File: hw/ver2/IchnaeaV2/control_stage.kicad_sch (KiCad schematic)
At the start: 119 parts, among them J5 FanConnector, J6 BMS_Serial, P1 USB_C_Plug_USB2.0, Q26 BSS138, Q27 BSS84, Q28 BSS138, Q29 BSS138, Q30 BSS138, SW1 Boot, SW2 Reset, U10 W25Q32JVZP, U11 RP2040, U12 LM1117MP-5.0, U13 LM1117MP-3.3, U14 W25Q32JVZP, U9 74HC4051PW, Y1 12MHz

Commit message: Partial pin mapping. ESD protection on signals that exit the board.
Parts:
- removed R85: 1k, Resistor_SMD:R_0603_1608Metric, symbol Device:R_US
- added C111: 100nF, Capacitor_SMD:C_0603_1608Metric, symbol Device:C
- added D11, D12, D13, D14, D15, D16, D17, D18, D9: ESD9B3.3ST5G, Diode_SMD:D_SOD-923, symbol Diode:ESD9B3.3ST5G
- added D19, D20: ESD9B5.0ST5G, Diode_SMD:D_SOD-923, symbol Diode:ESD9B5.0ST5G
- added J7: BMS_Serial, Connector_Harwin:Harwin_M20-89003xx_1x03_P2.54mm_Horizontal, symbol Connector:Conn_01x03_Pin
- added JP1, JP2, JP3, JP4: SolderJumper_3_Bridged12, Jumper:SolderJumper-3_P1.3mm_Bridged12_Pad1.0x1.5mm, symbol Jumper:SolderJumper_3_Bridged12
- added R121, R122, R123: 100, Resistor_SMD:R_0603_1608Metric, symbol Device:R_US
- R100, R101, R97: value 1k -> 100; LCSC C21190 -> C22775
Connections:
- net +3.3V: now also U14.3 (IO2), U14.7 (IO3), U14.8 (VCC), C111.1, D18.2 (A2)
- net CTL_IN_SDI: now also JP2.2 (C); no longer U11.15 (GPIO12)
- net CTL_OUT_SDO: now also JP1.2 (C); no longer U11.14 (GPIO11)
- net FAN_CTL: now also D14.2 (A2)
- net FAN_SENSE: now also D15.2 (A2), R123.1; no longer J5.3 (Pin_3)
- net GND: now also U14.4 (GND), U14.9 (EP), C111.2, D11.1 (A1), D12.1 (A1), D13.1 (A1), D14.1 (A1), D15.1 (A1), D16.1 (A1), D17.1 (A1), D18.1 (A1), D19.2 (A2), D20.2 (A2), D9.1 (A1), J7.3 (Pin_3)
- net RUN: now also D17.2 (A2)
- net UART0_RX: now also D12.2 (A2), R122.2; no longer R101.2
- net UART0_TX: now also D13.2 (A2), R121.2; no longer R100.2
- net USB_D+: now also D20.1 (A1)
- net USB_D-: now also D19.1 (A1)
- net SPI0_CSn: now reaches U14.1 (~{CS})
- net SPI0_CSn: now also U11.3 (GPIO1)
- net NOR_DO: now reaches U14.2 (DO(IO1))
- net NOR_DO: now also JP3.2 (C)
- net NOR_DI: now reaches U14.5 (DI(IO0))
- net NOR_DI: now also JP4.2 (C)
- net SPI0_SCK: now reaches U14.6 (CLK)
- net SPI0_SCK: now also U11.4 (GPIO2)
- net at R84.1, SW1.2: now also D16.2 (A2)
- net UART1_TX: now reaches U11.31 (GPIO20)
- net UART1_TX: now also R100.2, D9.2 (A2)
- net UART1_RX: now reaches U11.32 (GPIO21)
- net UART1_RX: now also R101.2, D11.2 (A2)
- net SPI0_TX: now reaches U11.5 (GPIO3)
- net SPI0_RX: now reaches U11.6 (GPIO4)
- net SPI0_RX: now also JP3.1 (A), JP4.3 (B)
- net CTL_RUN: no longer names the net of U11.37 (GPIO25)
- new net: J5.3 (Pin_3), R123.2
- new net: J7.1 (Pin_1), R121.1
- new net: J7.2 (Pin_2), R122.1
- new net SPI1_RX: JP1.3 (B), JP2.1 (A), U11.15 (GPIO12)
- new net SPI1_TX: JP1.1 (A), JP2.3 (B), JP3.3 (B), JP4.1 (A), U11.14 (GPIO11)
- no-connect marks 5 -> 6
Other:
- note added: "Invertible SPI"
- note added: "Routing Suggestion: https://electronics.stackexchange.com/q/585993"
- note removed: "LTC_CCM"
- note removed: "LTC_DCM"
- note removed: "TODO: Make a spreadsheet for pin mappings"
- moved on the sheet: C23, J5, R84, R89, R90, R92, R96, R97, SW1, SW2

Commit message: More routing considerations for logic stage
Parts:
- removed D2, D3: Yellow LED, LED_SMD:LED_0805_2012Metric, symbol Device:LED
- removed R53, R55: 10k, Resistor_SMD:R_0603_1608Metric, symbol Device:R_US
- added TP71: TestPoint, TestPoint:TestPoint_Pad_D1.0mm, symbol Connector:TestPoint
- J6: value BMS_Serial -> Debug; footprint Connector_Harwin:Harwin_M20-89003xx_1x03_P2.54mm_Horizontal -> Connector_PinHeader_2.54mm:PinHeader_1x03_P2.54mm_Vertical; Digikey 952-3232-ND -> N/A
- J7: footprint Connector_Harwin:Harwin_M20-89003xx_1x03_P2.54mm_Horizontal -> Connector_PinHeader_2.54mm:PinHeader_1x03_P2.54mm_Vertical; Digikey 952-3232-ND -> N/A
- JP1, JP2, JP3, JP4: footprint Jumper:SolderJumper-3_P1.3mm_Bridged12_Pad1.0x1.5mm -> Jumpers:JumperSolderJumper-3_P0.5mm_Bridged12_0603
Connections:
- net +3.3V: now also R102.1, R103.1, TP71.1
- net +5V: no longer R102.1, R103.1
- net CTL_OUT_SCK: now also U11.17 (GPIO14); no longer U11.13 (GPIO10)
- net SPI0_RX: now also U11.2 (GPIO0); no longer U11.6 (GPIO4)
- net SPI1_TX: now also U11.18 (GPIO15); no longer U11.14 (GPIO11)
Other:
- moved on the sheet: C23, D11, D12, D13, D16, D17, D9, J6, J7, Q26, Q27, Q28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

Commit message: Sync work
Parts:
- added D2, D21, D24, D3: ESD9B5.0ST5G, Diode_SMD:D_SOD-923, symbol Diode:ESD9B5.0ST5G
- added Q31, Q32, Q33, Q34: BSS138, Package_TO_SOT_SMD:SOT-23, symbol Transistor_FET:BSS138
- added R106, R125, R127, R129: 10k, Resistor_SMD:R_0603_1608Metric, symbol Device:R_US
- added R124, R126, R128, R94: 100, Resistor_SMD:R_0603_1608Metric, symbol Device:R_US
- added TP72, TP73, TP74: TestPoint, TestPoint:TestPoint_Pad_D1.0mm, symbol Connector:TestPoint
- R78, R81: footprint Resistor_SMD:R_0603_1608Metric -> Resistor_SMD:R_0805_2012Metric; LCSC C23178 -> C17709
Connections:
- net +3.3V: now also D24.1 (A1)
- net ADC_SEL_0: now also U11.8 (GPIO6)
- net ADC_SEL_1: now also U11.7 (GPIO5)
- net ADC_SEL_2: now also U11.6 (GPIO4)
- net CTL_LTC_PWM_EN: now also U11.14 (GPIO11)
- net FAN_CTL: now also U11.36 (GPIO24); no longer U11.34 (GPIO22)
- net FAN_SENSE: now also U11.37 (GPIO25); no longer U11.35 (GPIO23)
- net GND: now also D2.2 (A2), D21.2 (A2), D24.2 (A2), D3.2 (A2), Q31.2 (S), Q32.2 (S), Q33.2 (S), Q34.2 (S), R106.1, R125.1, R127.1, R129.1, TP72.1
- net LED_STATUS_0: now also U11.29 (GPIO18), R128.2; no longer D5.1 (K)
- net LED_STATUS_1: now also U11.30 (GPIO19), R126.2; no longer D6.1 (K)
- net LED_STATUS_2: now also U11.34 (GPIO22), R124.2; no longer D7.1 (K)
- net LED_STATUS_3: now also U11.35 (GPIO23), R94.2; no longer D8.1 (K)
- net LTC_CCM: now also U11.11 (GPIO8)
- net LTC_DCM: now also U11.12 (GPIO9)
- net LTC_RUN: now also U11.9 (GPIO7)
- net LTC_SYNC: now also U11.13 (GPIO10)
- net RUN: now also D2.1 (A1), TP73.1
- net SWCLK: now also D3.1 (A1)
- net SWDATA: now also D21.1 (A1)
- net USB_D+: now also R99.1, U11.47 (USB_DP); no longer D20.1 (A1), P1.A6 (D+), P1.B6 (D+), R98.2
- net USB_D-: now also R98.1, U11.46 (USB_DM); no longer D19.1 (A1), P1.A7 (D-), P1.B7 (D-), R99.2
- net at D16.2 (A2), R84.1, SW1.2: now also TP74.1
- new net: D20.1 (A1), P1.A6 (D+), P1.B6 (D+), R99.2
- new net: Q33.1 (G), R124.1, R125.2
- new net: Q32.1 (G), R126.1, R127.2
- new net: D6.1 (K), Q32.3 (D)
- new net: Q31.1 (G), R128.1, R129.2
- new net: D5.1 (K), Q31.3 (D)
- new net: Q34.1 (G), R106.2, R94.1
- new net: D19.1 (A1), P1.A7 (D-), P1.B7 (D-), R98.2
- new net: D8.1 (K), Q34.3 (D)
- new net: D7.1 (K), Q33.3 (D)
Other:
- note removed: "Routing Suggestion: https://electronics.stackexchange.com/q/585993"
- moved on the sheet: C111, C23, D11, D12, D13, D14, D15, D16, D17, D5, D6, D7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

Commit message: Sync to main pc
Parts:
- removed C92: 100nF, Capacitor_SMD:C_0603_1608Metric, symbol Device:C
- added TP75, TP76: TestPoint, TestPoint:TestPoint_Pad_D1.0mm, symbol Connector:TestPoint
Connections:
- net SPI0_RX is gone; now on net NOR_DO: JP3.1 (A), JP4.3 (B), U11.2 (GPIO0)
- net SPI0_TX is gone; now on net NOR_DI: U11.5 (GPIO3)
- net CTL_OUT_SDO: now also JP1.1 (A), JP2.3 (B), U11.18 (GPIO15)
- net NOR_DI: now also JP3.3 (B), JP4.1 (A)
- net at C49.2, U11.20 (XIN), Y1.1: now also TP75.1
- net at R95.2, U11.21 (XOUT): now also TP76.1
- removed net SPI1_TX: JP1.1 (A), JP2.3 (B), JP3.3 (B), JP4.1 (A), U11.18 (GPIO15)
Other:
- moved on the sheet: C94

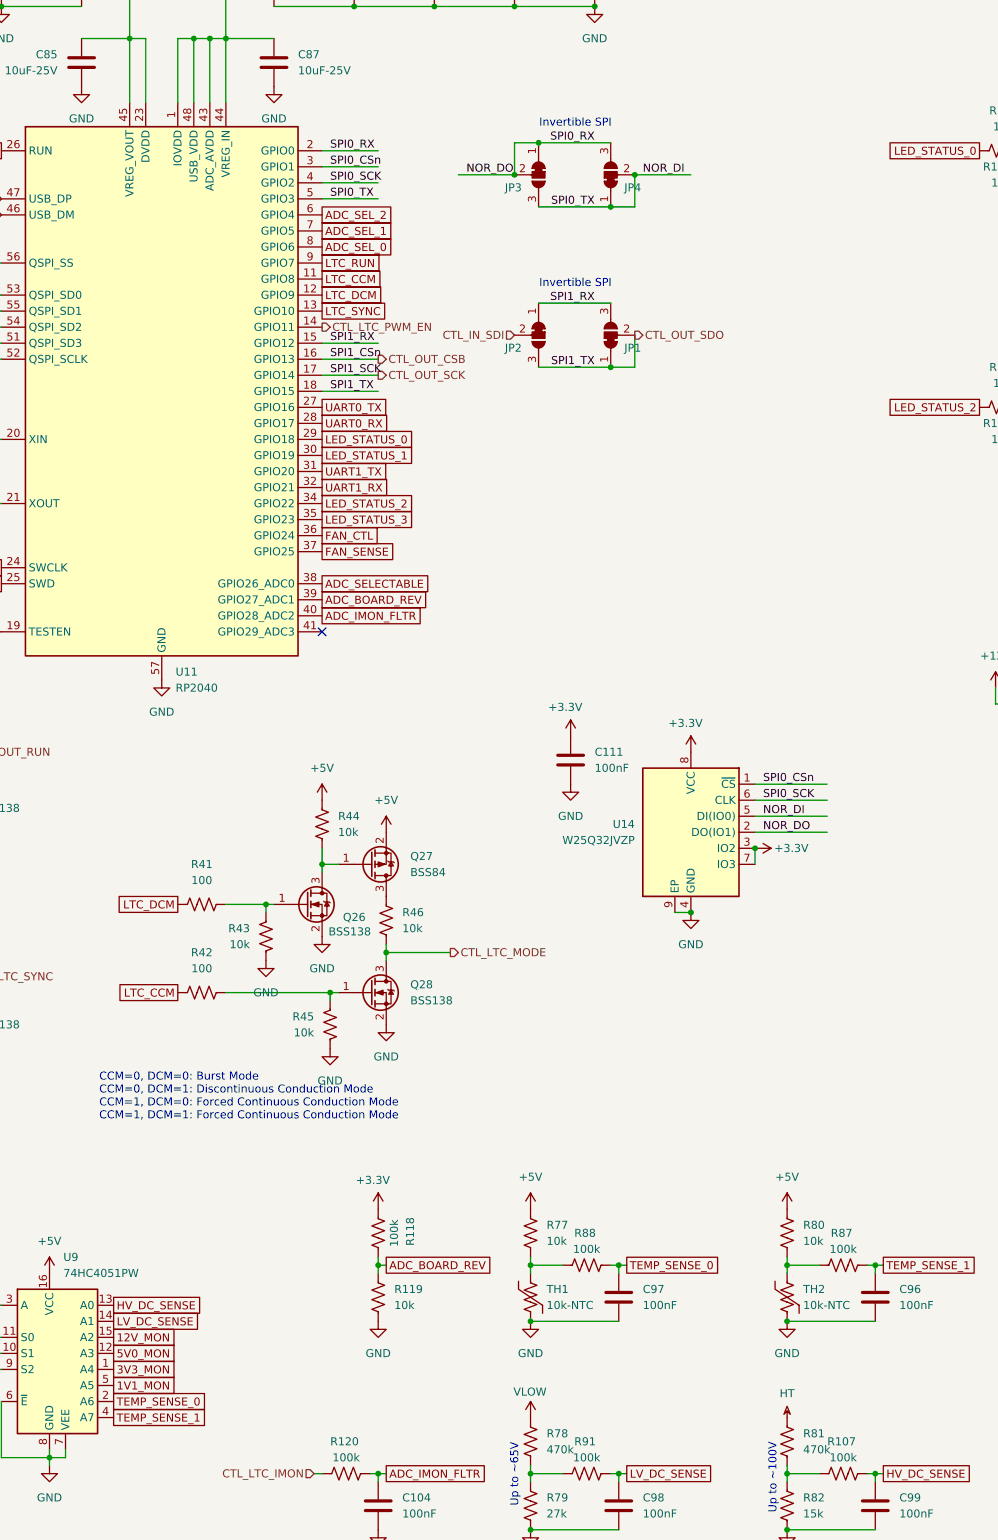
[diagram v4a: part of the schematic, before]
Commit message: Finish the initial rough route/placement
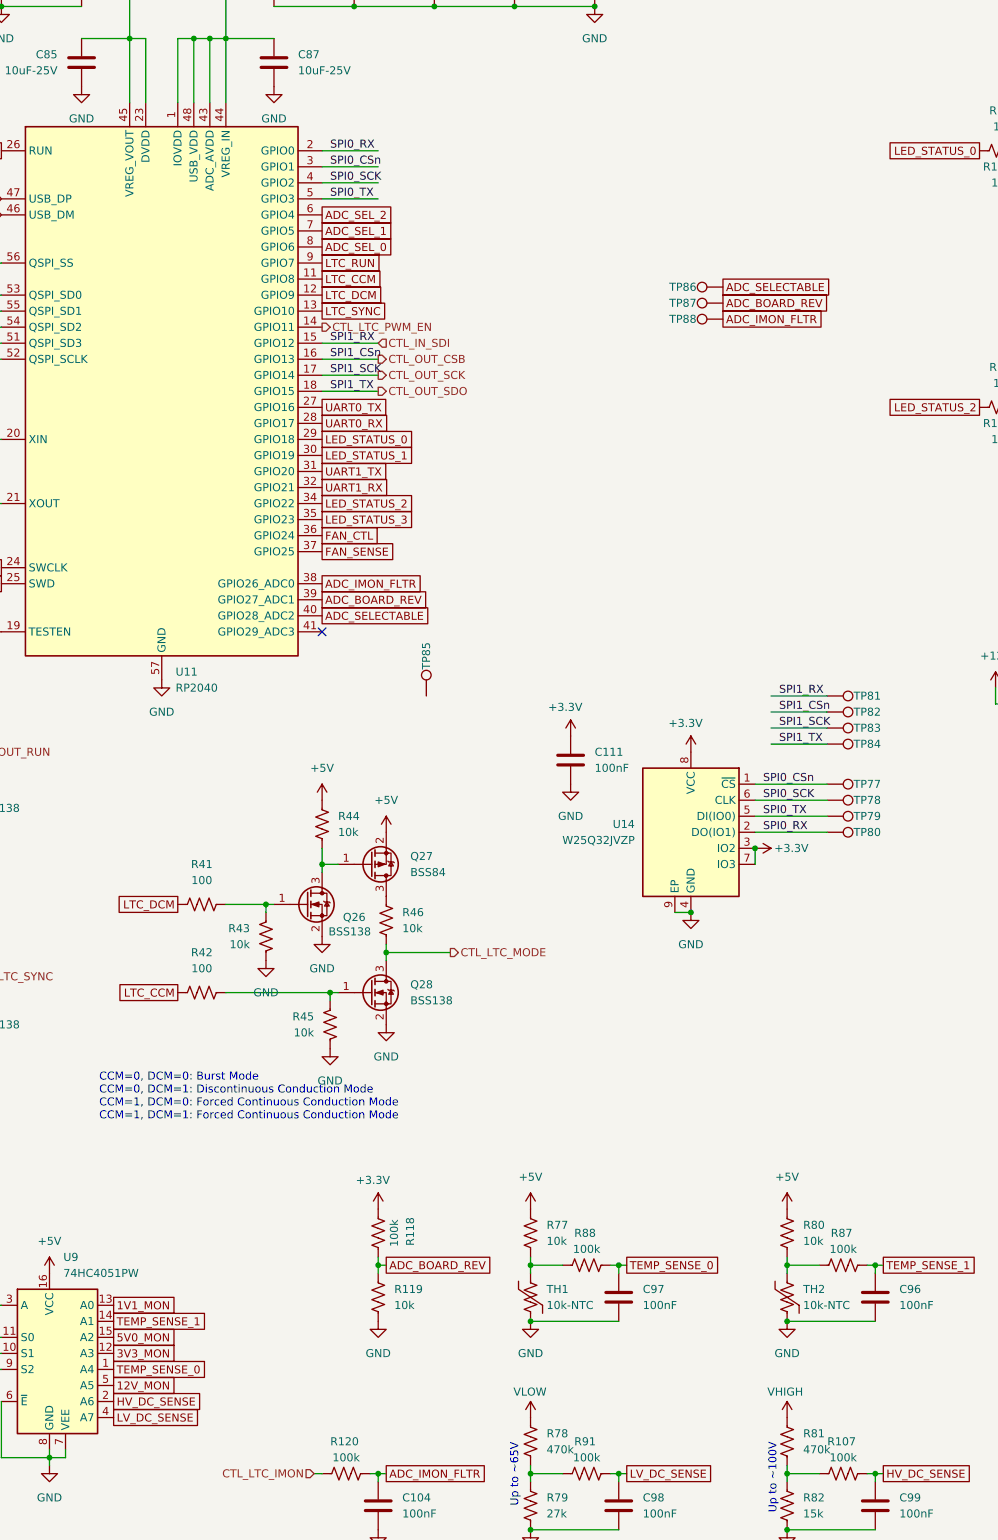
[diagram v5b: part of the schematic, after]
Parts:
- removed JP1, JP2, JP3, JP4: SolderJumper_3_Bridged12, Jumpers:JumperSolderJumper-3_P0.5mm_Bridged12_0603, symbol Jumper:SolderJumper_3_Bridged12
- added TP77, TP78, TP79, TP80, TP81, TP82, TP83, TP84, TP85, TP86, TP87, TP88: TestPoint, TestPoint:TestPoint_Pad_D1.0mm, symbol Connector:TestPoint
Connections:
- net SPI1_RX is gone; now on net CTL_IN_SDI: U11.15 (GPIO12)
- net 12V_MON: now also U9.5 (A5); no longer U9.15 (A2)
- net 1V1_MON: now also U9.13 (A0); no longer U9.5 (A5)
- net 3V3_MON: now also U9.12 (A3); no longer U9.1 (A4)
- net 5V0_MON: now also U9.15 (A2); no longer U9.12 (A3)
- net ADC_BOARD_REV: now also TP87.1
- net ADC_IMON_FLTR: now also U11.38 (GPIO26_ADC0), TP88.1; no longer U11.40 (GPIO28_ADC2)
- net ADC_SELECTABLE: now also U11.40 (GPIO28_ADC2), TP86.1; no longer U11.38 (GPIO26_ADC0)
- net CTL_IN_SDI: now also TP81.1
- net CTL_OUT_CSB: now also TP82.1
- net CTL_OUT_SCK: now also TP83.1
- net CTL_OUT_SDO: now also TP84.1
- net HV_DC_SENSE: now also U9.2 (A6); no longer U9.13 (A0)
- net LV_DC_SENSE: now also U9.4 (A7); no longer U9.14 (A1)
- net SPI0_CSn: now also TP77.1
- net SPI0_SCK: now also TP78.1
- net TEMP_SENSE_0: now also U9.1 (A4); no longer U9.2 (A6)
- net TEMP_SENSE_1: now also U9.14 (A1); no longer U9.4 (A7)
- net HT renamed VHIGH
- net NOR_DI renamed SPI0_TX
- net SPI0_TX: now also TP79.1
- net NOR_DO renamed SPI0_RX
- net SPI0_RX: now also TP80.1
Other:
- note removed: "Invertible SPI"

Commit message: Finish routing V2
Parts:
- removed TP67: TestPoint, TestPoint:TestPoint_Pad_D1.0mm, symbol Connector:TestPoint
- added TP89, TP90, TP91, TP92, TP93, TP94, TP95: TestPoint, TestPoint:TestPoint_Pad_D1.0mm, symbol Connector:TestPoint
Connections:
- net 12V_MON: now also TP92.1
- net 1V1_MON: now also TP95.1
- net 3V3_MON: now also TP94.1
- net 5V0_MON: now also U9.14 (A1), TP93.1; no longer U9.15 (A2)
- net ADC_BOARD_REV: now also U11.40 (GPIO28_ADC2); no longer U11.39 (GPIO27_ADC1)
- net ADC_SELECTABLE: now also U11.39 (GPIO27_ADC1); no longer U11.40 (GPIO28_ADC2)
- net HV_DC_SENSE: now also TP91.1
- net LV_DC_SENSE: now also TP89.1
- net TEMP_SENSE_0: now also TP85.1
- net TEMP_SENSE_1: now also U9.15 (A2), TP90.1; no longer U9.14 (A1)
- net CTL_IN_ADC_IBATT_SENSE: now reaches U11.41 (GPIO29_ADC3)
- no-connect marks 6 -> 5
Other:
- moved on the sheet: TP85, TP86, TP87, TP88

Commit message: Test production outputs for V2
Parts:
- J4: value ~ -> SWD Debug; LCSC (none) -> N/A
- P1: LCSC N/A -> C7095263
- Q26, Q28, Q29, Q30, Q31, Q32, Q33, Q34: LCSC N/A -> C5224260
- Q27: LCSC N/A -> C2926187
- SW1, SW2: LCSC N/A -> C2915169
- TH1, TH2: LCSC N/A -> C333993
- TP64, TP65, TP66, TP68, TP69, TP70, TP71, TP72, TP73, TP74, TP75, TP76, TP77, TP78, TP79, TP80, TP81, TP82, TP83, TP84, TP85, TP86, TP87, TP88, TP89, TP90, TP91, TP92, TP93, TP94, TP95: LCSC (none) -> N/A
- U10, U14: LCSC N/A -> C571260
- U9: LCSC N/A -> C19723805
- Y1: LCSC N/A -> C7294550
